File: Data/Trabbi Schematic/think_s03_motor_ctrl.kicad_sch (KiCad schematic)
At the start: 9 parts, among them K1 Start Inhibit Relay B, K2 Radiator Fan Relay (R11), K3 Gear Lock Relay R8, K4 Gear Lock Relay R9, K5 Gear Lock Relay R10, M1 Gear Lock Motor E20/E21, SW1 Brake Light Switch (C12), U1 Motor Controller E01 Signals, U2 BMS (E02)

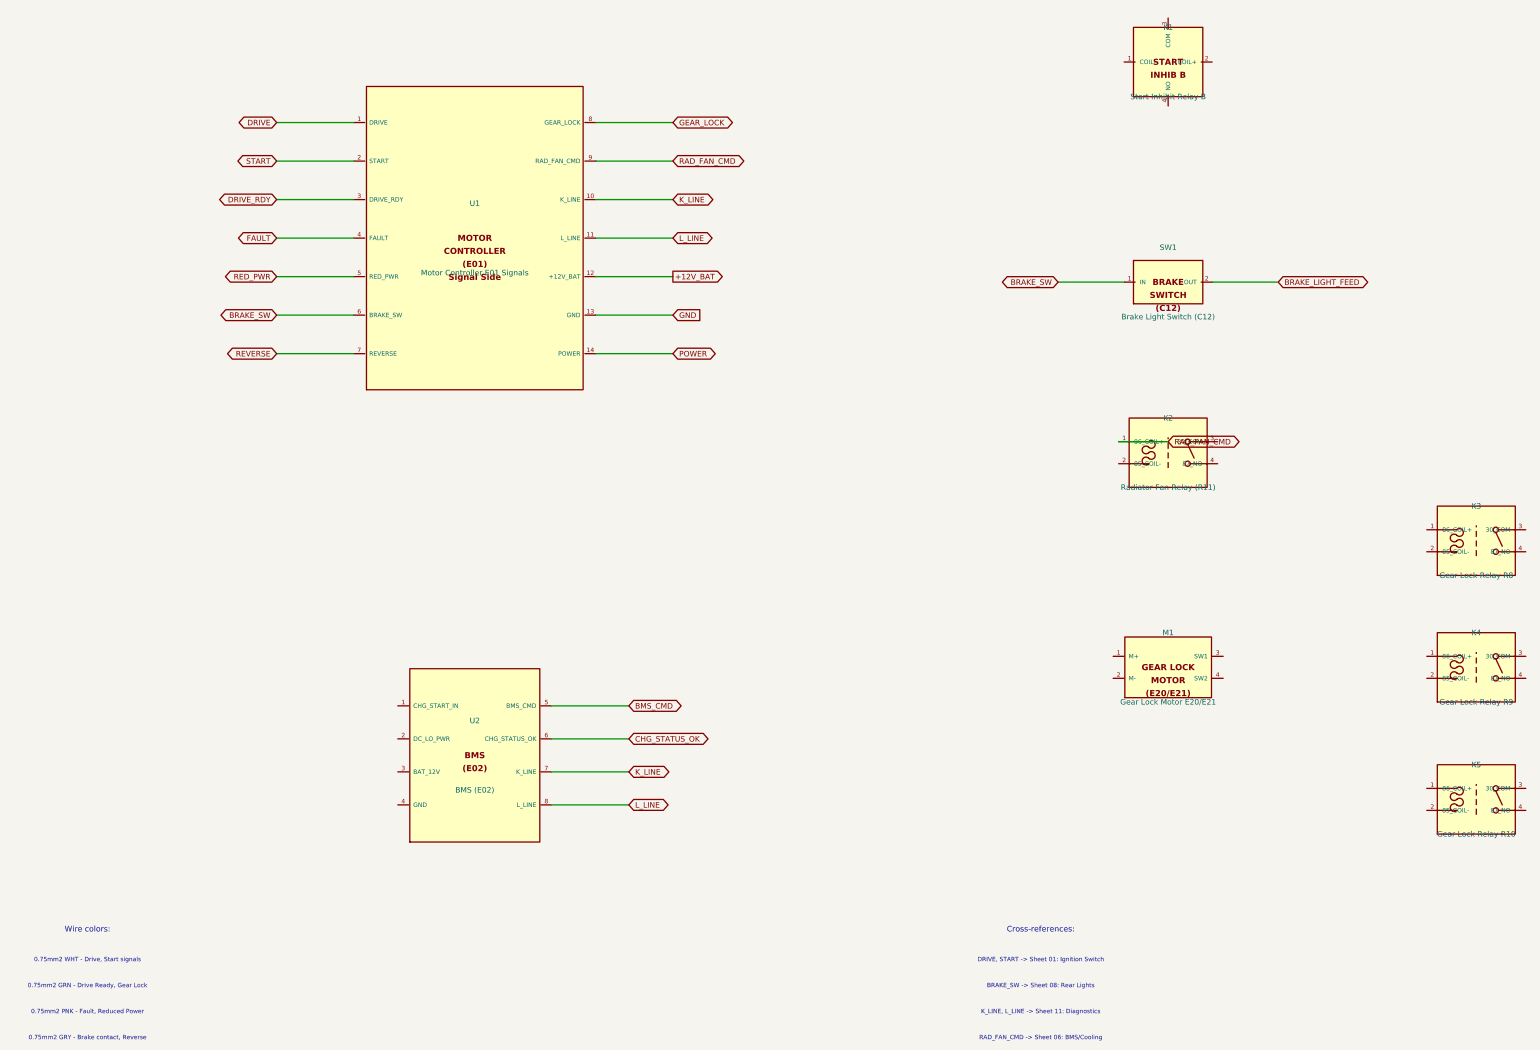
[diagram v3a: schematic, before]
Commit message: Fix label/text positioning: Ref/Value outside body, hide pin numbers
- Reference placed above body edge, Value below (dynamic based on
  symbol height) — no longer overlapping body text
- Pin numbers hidden (clutter, not useful in schematic view)
- Pin name font reduced from 1.016mm to 0.762mm (less overlap)
- Pin length increased from 2.54mm to 3.81mm (more room for pin names
  between body edge and endpoint)
- Store symbol dimensions in _sym_dims for dynamic property placement

Co-Authored-By: Claude Opus 4.6 <noreply@anthropic.com>
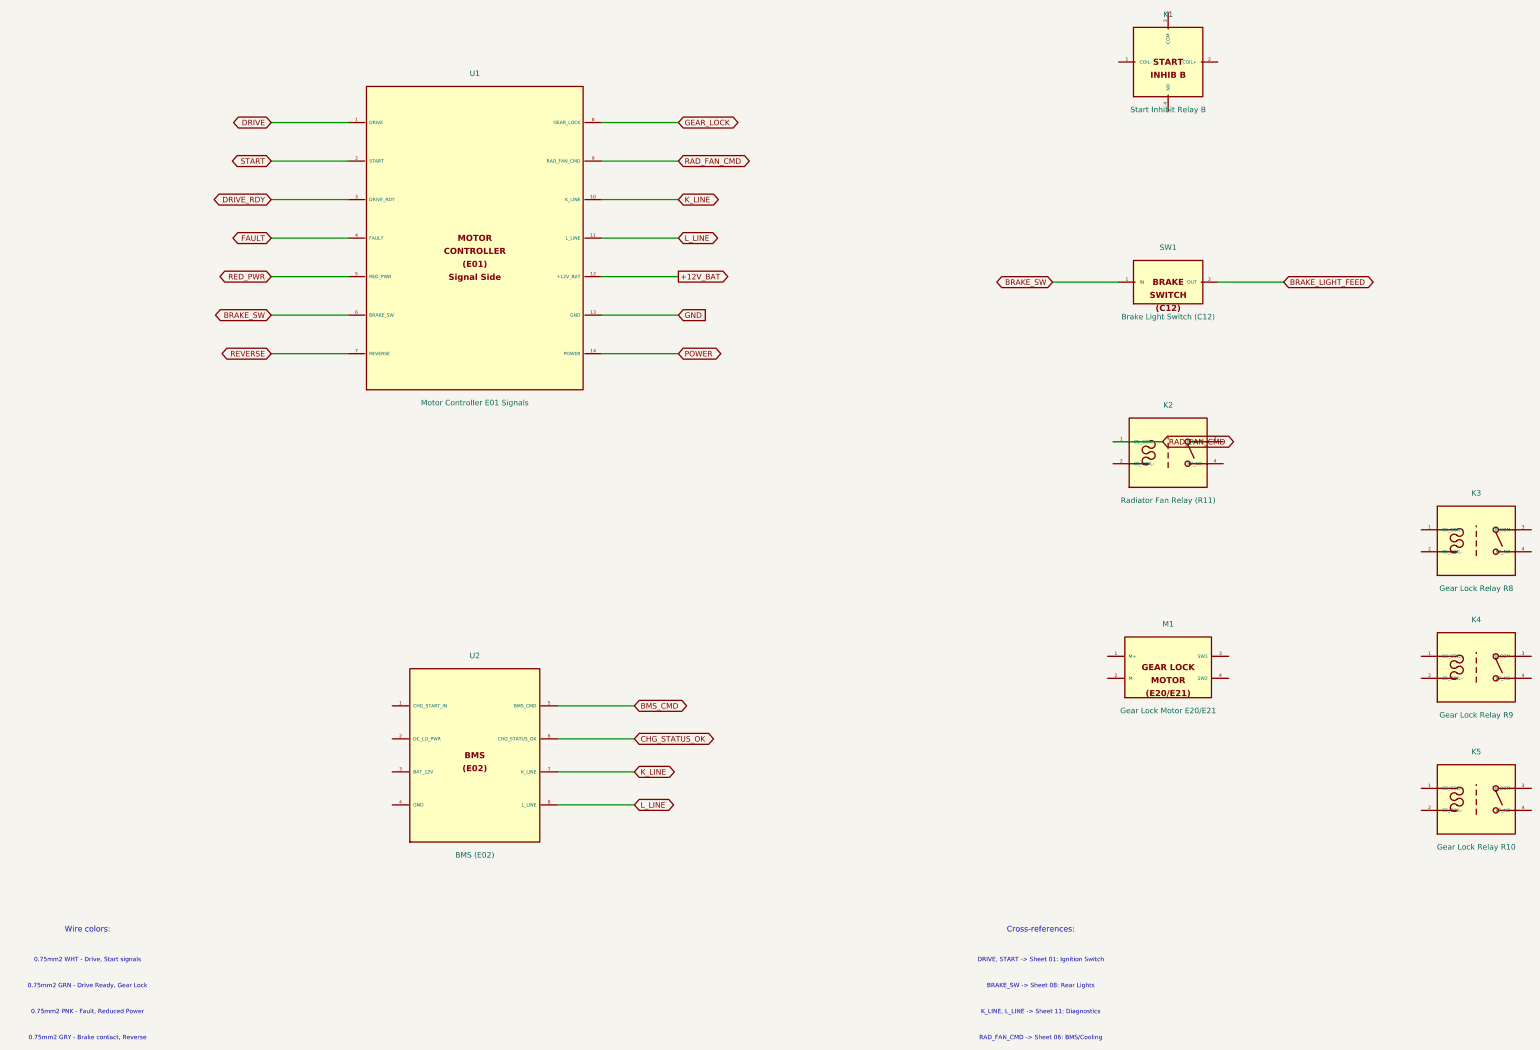
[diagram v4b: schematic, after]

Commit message: Add cross-sheet reference annotations to global labels
- Track all global label positions per sheet during build
- After building all sheets, annotate each global label with
  "→S01,S03,..." text showing which other sheets share the net
- 60 cross-sheet nets identified and annotated
- Two-pass build: 1) build all sheets 2) add cross-refs + save
- Text placed near label in 0.8mm font, offset to avoid overlap

Co-Authored-By: Claude Opus 4.6 <noreply@anthropic.com>
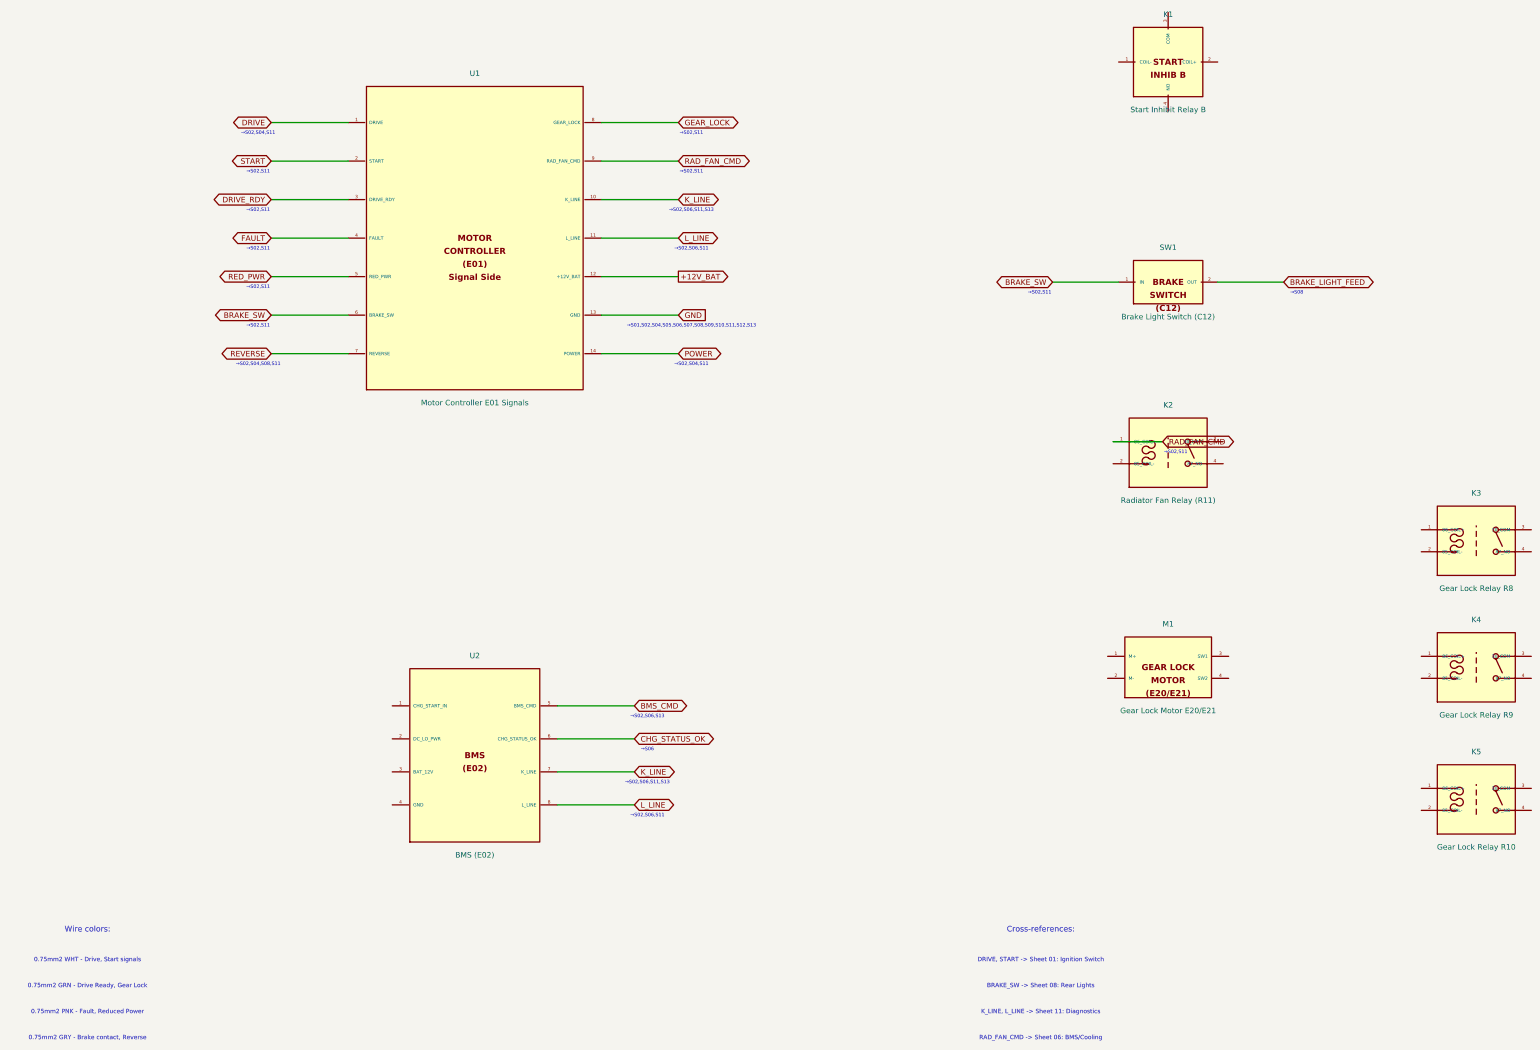
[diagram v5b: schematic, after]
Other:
- note added: "→S01,S02,S04,S05,S06,S07,S08,S09,S10,S11,S12,S13"
- note added: "→S02,S04,S08,S11"
- note added: "→S02,S04,S11"
- note added: "→S02,S06,S11"
- note added: "→S02,S06,S11,S13"
- note added: "→S02,S06,S13"
- note added: "→S02,S11"
- note added: "→S06"
- note added: "→S08"
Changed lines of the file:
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@@
     (effects (font (size 1.000 1.000)))
+  )
+  (text "→S02,S04,S11" (at 69.390 76.160 0)
+    (effects (font (size 0.800 0.800)))
+  )
+  (text "→S02,S11" (at 69.390 85.050 0)
+    (effects (font (size 0.800 0.800)))
+  )
+  (text "→S02,S11" (at 69.390 93.940 0)
+    (effects (font (size 0.800 0.800)))
+  )
+  (text "→S02,S11" (at 69.390 102.830 0)
+    (effects (font (size 0.800 0.800)))
+  )
+  (text "→S02,S11" (at 69.390 111.720 0)
+    (effects (font (size 0.800 0.800)))
+  )
+  (text "→S02,S11" (at 69.390 120.610 0)
+    (effects (font (size 0.800 0.800)))
+  )
+  (text "→S02,S11" (at 249.730 112.990 0)
+    (effects (font (size 0.800 0.800)))
+  )
+  (text "→S02,S04,S08,S11" (at 69.390 129.500 0)
+    (effects (font (size 0.800 0.800)))
+  )
+  (text "→S02,S11" (at 169.370 76.160 0)
+    (effects (font (size 0.800 0.800)))
+  )
+  (text "→S02,S11" (at 169.370 85.050 0)
+    (effects (font (size 0.800 0.800)))
+  )
+  (text "→S02,S11" (at 281.130 149.820 0)
+    (effects (font (size 0.800 0.800)))
+  )
+  (text "→S02,S06,S11,S13" (at 169.370 93.940 0)
+    (effects (font (size 0.800 0.800)))
+  )
+  (text "→S02,S06,S11,S13" (at 159.210 226.020 0)
+    (effects (font (size 0.800 0.800)))
+  )
+  (text "→S02,S06,S11" (at 169.370 102.830 0)
+    (effects (font (size 0.800 0.800)))
+  )
+  (text "→S02,S06,S11" (at 159.210 233.640 0)
+    (effects (font (size 0.800 0.800)))
+  )
+  (text "→S01,S02,S04,S05,S06,S07,S08,S09,S10,S11,S12,S13" (at 169.370 120.610 0)
+    (effects (font (size 0.800 0.800)))
+  )
+  (text "→S02,S04,S11" (at 169.370 129.500 0)
+    (effects (font (size 0.800 0.800)))
+  )
+  (text "→S02,S06,S13" (at 159.210 210.780 0)
+    (effects (font (size 0.800 0.800)))
+  )
+  (text "→S06" (at 159.210 218.400 0)
+    (effects (font (size 0.800 0.800)))
+  )
+  (text "→S08" (at 309.070 112.990 0)
+    (effects (font (size 0.800 0.800)))
   )
   (symbol_instances)

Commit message: Fix label text justification for KiCad 9
Add (justify left) to all label and global_label effects.
KiCad 9 requires explicit text justification — without it,
label text is mispositioned relative to the label shape.

Co-Authored-By: Claude Opus 4.6 <noreply@anthropic.com>
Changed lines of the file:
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@@
   )
   (global_label "DRIVE" (shape bidirectional) (at 72.390 73.660 180)
-    (effects (font (size 1.27 1.27)))
+    (effects (font (size 1.27 1.27)) (justify left))
     (property "Intersheetrefs" "${INTERSHEET_REFS}" (at 72.390 73.660 0)
       (effects (font (size 1.27 1.27)) hide)
@@
   )
   (global_label "START" (shape bidirectional) (at 72.390 82.550 180)
-    (effects (font (size 1.27 1.27)))
+    (effects (font (size 1.27 1.27)) (justify left))
     (property "Intersheetrefs" "${INTERSHEET_REFS}" (at 72.390 82.550 0)
       (effects (font (size 1.27 1.27)) hide)
@@
   )
   (global_label "DRIVE_RDY" (shape bidirectional) (at 72.390 91.440 180)
-    (effects (font (size 1.27 1.27)))
+    (effects (font (size 1.27 1.27)) (justify left))
     (property "Intersheetrefs" "${INTERSHEET_REFS}" (at 72.390 91.440 0)
       (effects (font (size 1.27 1.27)) hide)
@@
   )
   (global_label "FAULT" (shape bidirectional) (at 72.390 100.330 180)
-    (effects (font (size 1.27 1.27)))
+    (effects (font (size 1.27 1.27)) (justify left))
     (property "Intersheetrefs" "${INTERSHEET_REFS}" (at 72.390 100.330 0)
       (effects (font (size 1.27 1.27)) hide)
@@
   )
   (global_label "RED_PWR" (shape bidirectional) (at 72.390 109.220 180)
-    (effects (font (size 1.27 1.27)))
+    (effects (font (size 1.27 1.27)) (justify left))
     (property "Intersheetrefs" "${INTERSHEET_REFS}" (at 72.390 109.220 0)
       (effects (font (size 1.27 1.27)) hide)
@@
   )
   (global_label "BRAKE_SW" (shape bidirectional) (at 72.390 118.110 180)
-    (effects (font (size 1.27 1.27)))
+    (effects (font (size 1.27 1.27)) (justify left))
     (property "Intersheetrefs" "${INTERSHEET_REFS}" (at 72.390 118.110 0)
       (effects (font (size 1.27 1.27)) hide)
@@
   )
   (global_label "REVERSE" (shape bidirectional) (at 72.390 127.000 180)
-    (effects (font (size 1.27 1.27)))
+    (effects (font (size 1.27 1.27)) (justify left))
     (property "Intersheetrefs" "${INTERSHEET_REFS}" (at 72.390 127.000 0)
       (effects (font (size 1.27 1.27)) hide)
@@
   )
   (global_label "GEAR_LOCK" (shape bidirectional) (at 166.370 73.660 0)
-    (effects (font (size 1.27 1.27)))
+    (effects (font (size 1.27 1.27)) (justify left))
     (property "Intersheetrefs" "${INTERSHEET_REFS}" (at 166.370 73.660 0)
       (effects (font (size 1.27 1.27)) hide)
@@
   )
   (global_label "RAD_FAN_CMD" (shape bidirectional) (at 166.370 82.550 0)
-    (effects (font (size 1.27 1.27)))
+    (effects (font (size 1.27 1.27)) (justify left))
     (property "Intersheetrefs" "${INTERSHEET_REFS}" (at 166.370 82.550 0)
       (effects (font (size 1.27 1.27)) hide)
@@
   )
   (global_label "K_LINE" (shape bidirectional) (at 166.370 91.440 0)
-    (effects (font (size 1.27 1.27)))
+    (effects (font (size 1.27 1.27)) (justify left))
     (property "Intersheetrefs" "${INTERSHEET_REFS}" (at 166.370 91.440 0)
       (effects (font (size 1.27 1.27)) hide)
@@
   )
   (global_label "L_LINE" (shape bidirectional) (at 166.370 100.330 0)
-    (effects (font (size 1.27 1.27)))
+    (effects (font (size 1.27 1.27)) (justify left))
     (property "Intersheetrefs" "${INTERSHEET_REFS}" (at 166.370 100.330 0)
       (effects (font (size 1.27 1.27)) hide)
@@
   )
   (global_label "+12V_BAT" (shape output) (at 166.370 109.220 0)
-    (effects (font (size 1.27 1.27)))
+    (effects (font (size 1.27 1.27)) (justify left))
     (property "Intersheetrefs" "${INTERSHEET_REFS}" (at 166.370 109.220 0)
       (effects (font (size 1.27 1.27)) hide)
@@
   )
   (global_label "GND" (shape input) (at 166.370 118.110 0)
-    (effects (font (size 1.27 1.27)))
+    (effects (font (size 1.27 1.27)) (justify left))
     (property "Intersheetrefs" "${INTERSHEET_REFS}" (at 166.370 118.110 0)
       (effects (font (size 1.27 1.27)) hide)
@@
   )
   (global_label "POWER" (shape bidirectional) (at 166.370 127.000 0)
-    (effects (font (size 1.27 1.27)))
+    (effects (font (size 1.27 1.27)) (justify left))
     (property "Intersheetrefs" "${INTERSHEET_REFS}" (at 166.370 127.000 0)
       (effects (font (size 1.27 1.27)) hide)
@@
   )
   (global_label "BMS_CMD" (shape bidirectional) (at 156.210 208.280 0)
-    (effects (font (size 1.27 1.27)))
+    (effects (font (size 1.27 1.27)) (justify left))
     (property "Intersheetrefs" "${INTERSHEET_REFS}" (at 156.210 208.280 0)
       (effects (font (size 1.27 1.27)) hide)
@@
   )
   (global_label "CHG_STATUS_OK" (shape bidirectional) (at 156.210 215.900 0)
-    (effects (font (size 1.27 1.27)))
+    (effects (font (size 1.27 1.27)) (justify left))
     (property "Intersheetrefs" "${INTERSHEET_REFS}" (at 156.210 215.900 0)
       (effects (font (size 1.27 1.27)) hide)
@@
   )
   (global_label "K_LINE" (shape bidirectional) (at 156.210 223.520 0)
-    (effects (font (size 1.27 1.27)))
+    (effects (font (size 1.27 1.27)) (justify left))
     (property "Intersheetrefs" "${INTERSHEET_REFS}" (at 156.210 223.520 0)
       (effects (font (size 1.27 1.27)) hide)
@@
   )
   (global_label "L_LINE" (shape bidirectional) (at 156.210 231.140 0)
-    (effects (font (size 1.27 1.27)))
+    (effects (font (size 1.27 1.27)) (justify left))
     (property "Intersheetrefs" "${INTERSHEET_REFS}" (at 156.210 231.140 0)
       (effects (font (size 1.27 1.27)) hide)
@@
   )
   (global_label "BRAKE_SW" (shape bidirectional) (at 252.730 110.490 180)
-    (effects (font (size 1.27 1.27)))
+    (effects (font (size 1.27 1.27)) (justify left))
     (property "Intersheetrefs" "${INTERSHEET_REFS}" (at 252.730 110.490 0)
       (effects (font (size 1.27 1.27)) hide)
@@
   )
   (global_label "BRAKE_LIGHT_FEED" (shape bidirectional) (at 306.070 110.490 0)
-    (effects (font (size 1.27 1.27)))
+    (effects (font (size 1.27 1.27)) (justify left))
     (property "Intersheetrefs" "${INTERSHEET_REFS}" (at 306.070 110.490 0)
       (effects (font (size 1.27 1.27)) hide)
@@
   )
   (global_label "RAD_FAN_CMD" (shape bidirectional) (at 278.130 147.320 0)
-    (effects (font (size 1.27 1.27)))
+    (effects (font (size 1.27 1.27)) (justify left))
     (property "Intersheetrefs" "${INTERSHEET_REFS}" (at 278.130 147.320 0)
       (effects (font (size 1.27 1.27)) hide)
